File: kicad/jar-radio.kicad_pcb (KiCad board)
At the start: 2 copper layers, 85.5 x 85.5 mm, 64 parts, among them J1 USB-C 5V, J2 BATT (PH), J3 ANT (XH), Q1 AO3401A, U1 Si4825-A10, U2 NS8002, U3 TP4056, U4 XC6206P332MR, U5 XC61CN2702MR, Y1 32.768kHz

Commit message: Speaker on PH socket, USB-C placed by JLC (two-sided), BOM/cost model/plan builder updates
Co-Authored-By: Claude Opus 5.5 <noreply@anthropic.com>
Claude-Session: https://claude.ai/code/session_01UChZ4MGw6SzykNSB399iC4
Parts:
- removed LS1: SPEAKER 8R, jar-radio:Speaker_Wire_Pads_P5
- added J4: SPK (PH), Connector_JST:JST_PH_B2B-PH-SM4-TB_1x02-1MP_P2.00mm_Vertical, B.Cu at (176.0, 100.2)
- moved C19 51.8 mm to (148.2, 133.1)
- moved C20 50.5 mm to (146.1, 133.2), turned to 90 degrees
- moved R14 47.3 mm to (150.6, 129.5)
- moved U3 36.3 mm to (168.2, 101.7), turned to 90 degrees
- moved C13 36.0 mm to (162.8, 131.9), turned to 0 degrees
- moved C12 35.5 mm to (152.5, 124.1)
- moved R12 31.2 mm to (181.6, 86.5)
- moved Q1 30.7 mm to (156.2, 132.9), turned to 0 degrees
- moved R5 20.8 mm to (183.2, 107.0)
- moved R11 19.0 mm to (177.4, 80.2), turned to 180 degrees
- moved C15 17.7 mm to (173.9, 80.0), turned to 0 degrees
- moved C11 15.0 mm to (175.1, 121.1)
- moved RV2 14.2 mm to (180.5, 107.0), turned to 180 degrees
- moved R4 14.1 mm to (163.0, 112.1)
- moved C10 13.4 mm to (182.0, 91.5)
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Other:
- board text added: "ANTENNA"
- board text added: "BATT +/-"
- board text added: "SPEAKER"

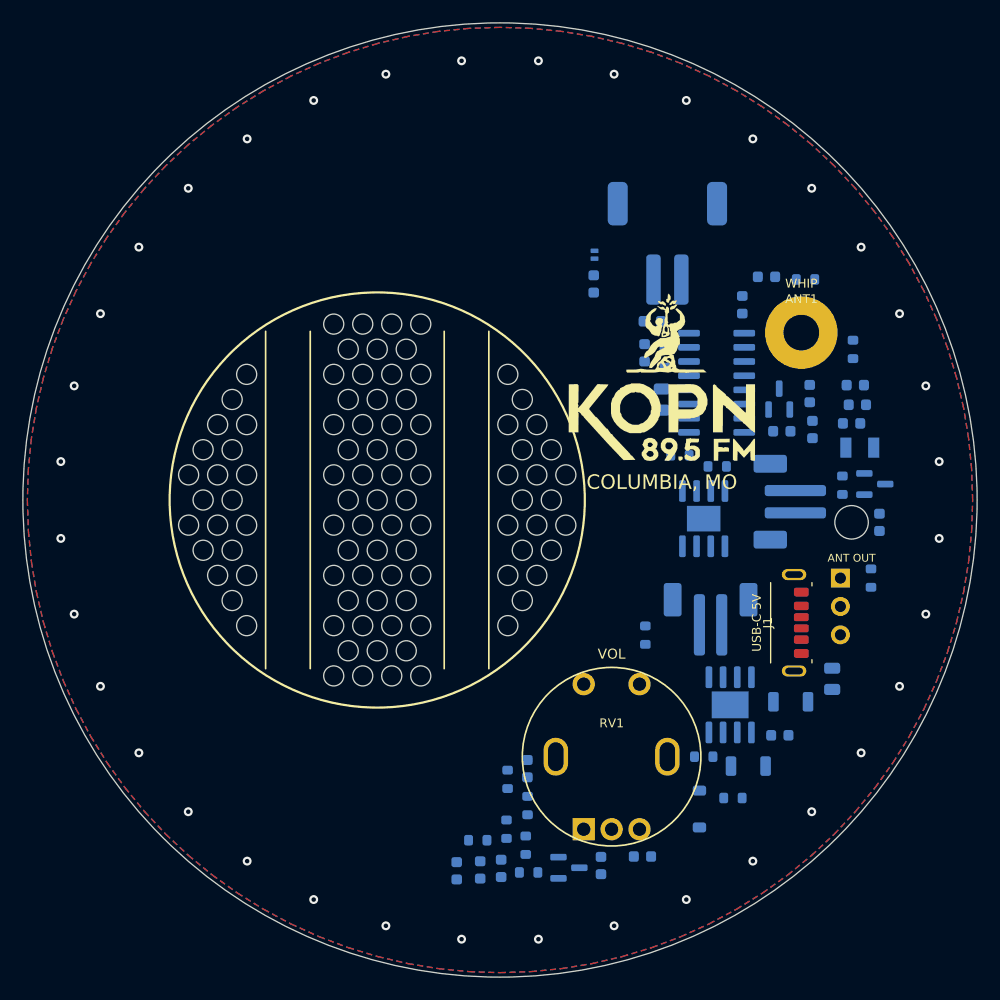
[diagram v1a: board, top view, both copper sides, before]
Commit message: Routed board rev A (one VSW connection still open); session re-import support
Co-Authored-By: Claude Opus 5.5 <noreply@anthropic.com>
Claude-Session: https://claude.ai/code/session_01UChZ4MGw6SzykNSB399iC4
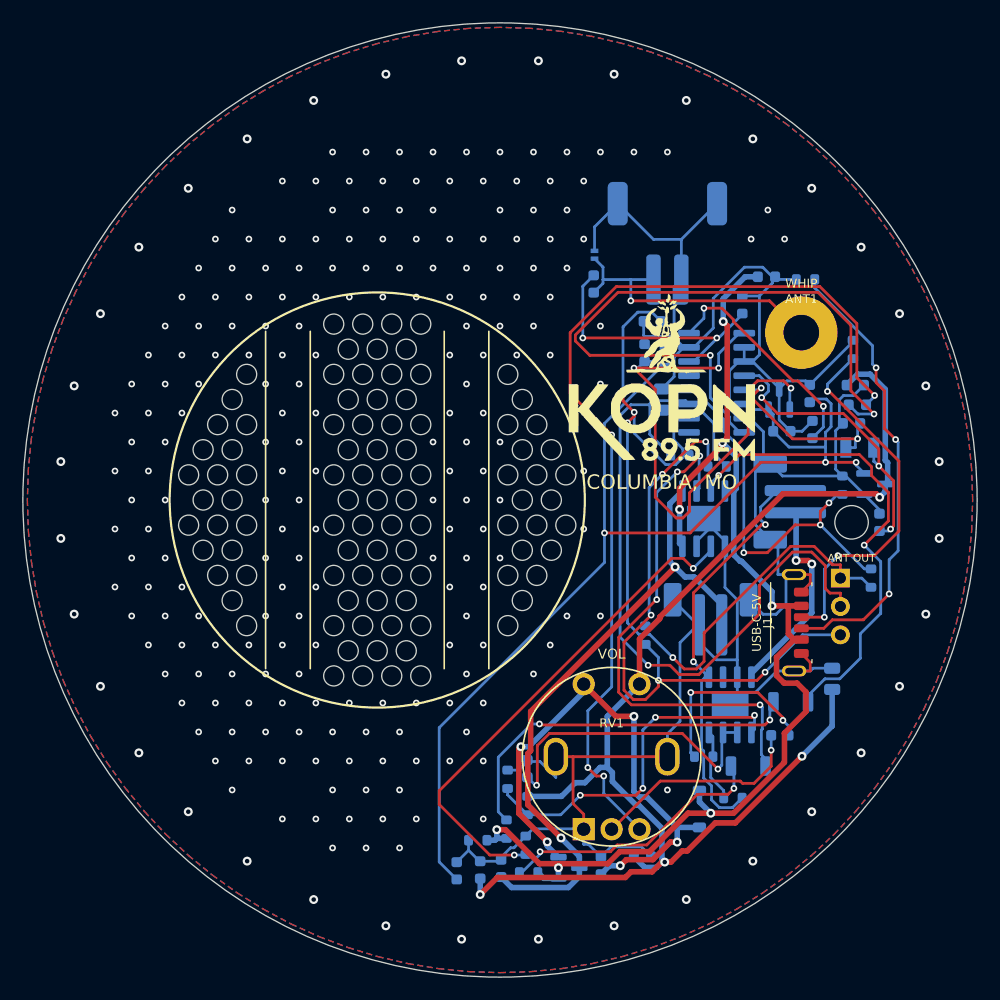
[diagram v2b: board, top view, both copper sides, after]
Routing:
- net GND: track 0.00 -> 246.2 mm, vias 36 -> 244
- net VSW: track 0.00 -> 119.1 mm, vias 0 -> 4
- net VBUS: track 0.00 -> 105.6 mm, vias 0 -> 7
- net +3V3: track 0.00 -> 99.0 mm, vias 0 -> 3
- net VOL_TOP: track 0.00 -> 86.3 mm, vias 0 -> 4
- net TUNE1: track 0.00 -> 78.1 mm, vias 0 -> 4
- net TUNE2: track 0.00 -> 70.4 mm, vias 0 -> 1
- net AOUT: track 0.00 -> 60.5 mm, vias 0 -> 2
- net VBAT: track 0.00 -> 57.8 mm, vias 0 -> 2
- net TUNE_LO: track 0.00 -> 54.5 mm, vias 0 -> 5
- net RST: track 0.00 -> 51.3 mm, vias 0 -> 3
- net VSYS: track 0.00 -> 48.8 mm, vias 0 -> 5
- net STDBY: track 0.00 -> 46.7 mm, vias 0 -> 4
- net PROG: track 0.00 -> 45.3 mm, vias 0 -> 2
- net CHRG: track 0.00 -> 43.3 mm, vias 0 -> 2
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
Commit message: WIP: clear stitching vias near the open VSW connection before final route
Co-Authored-By: Claude Opus 5.5 <noreply@anthropic.com>
Claude-Session: https://claude.ai/code/session_01UChZ4MGw6SzykNSB399iC4
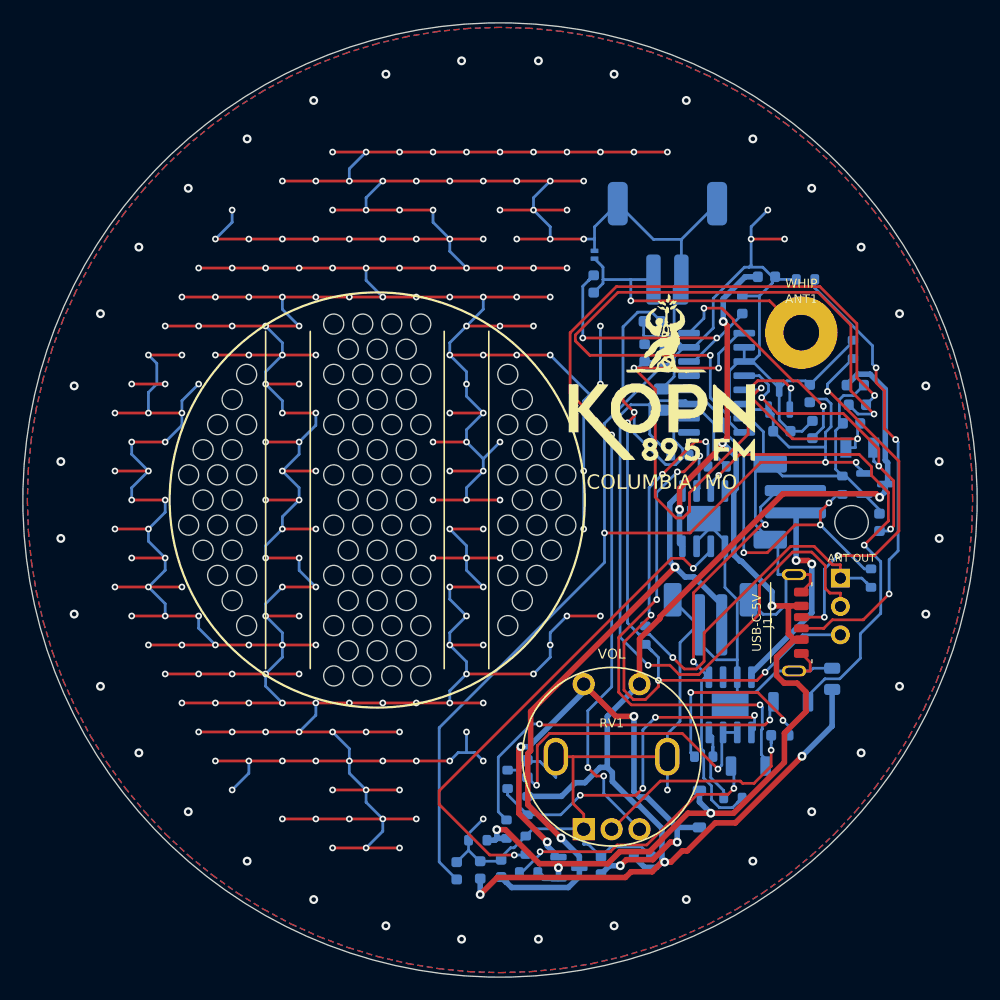
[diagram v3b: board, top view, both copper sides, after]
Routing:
- net GND: track 246.2 -> 893.1 mm
- net TUNE_LO: track 54.5 -> 55.8 mm
- net AMP_INN: track 6.59 -> 7.79 mm
- net VBAT: track 57.8 -> 58.6 mm
- net TUNE2: track 70.4 -> 71.1 mm
- net FMI: track 24.7 -> 25.3 mm
- net VOL_WIPER: track 19.6 -> 20.2 mm
- net XTALO: track 27.1 -> 27.7 mm
- net SPK+: track 37.7 -> 38.3 mm
- net TUNE1: track 78.1 -> 78.7 mm
- net LEDR_A: track 33.5 -> 34.0 mm
- net RST: track 51.3 -> 51.8 mm

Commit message: WIP board state during reroute
Co-Authored-By: Claude Opus 5.5 <noreply@anthropic.com>
Claude-Session: https://claude.ai/code/session_01UChZ4MGw6SzykNSB399iC4
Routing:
- net GND: track 893.1 -> 3.30 mm, vias 244 -> 271
- net AOUT: track 60.5 -> 11.8 mm
- net TUNE1: track 78.7 -> 39.1 mm, vias 4 -> 1
- net TUNE2: track 71.1 -> 31.7 mm
- net RST: track 51.8 -> 26.1 mm, vias 3 -> 4
- net TUNE_LO: track 55.8 -> 37.9 mm, vias 5 -> 3
- net VSYS: track 48.8 -> 32.6 mm, vias 5 -> 0
- net CHRG: track 43.6 -> 29.6 mm
- net VOL_TOP: track 86.3 -> 75.8 mm, vias 4 -> 2
- net VBAT: track 58.6 -> 68.0 mm, vias 2 -> 0
- net VSW: track 119.1 -> 111.5 mm, vias 4 -> 5
- net BAND: track 34.8 -> 27.6 mm, vias 3 -> 2
- net PROG: track 45.3 -> 38.8 mm
- net AMP_C: track 16.9 -> 10.7 mm
- net CC2: track 33.6 -> 39.8 mm, vias 3 -> 1
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
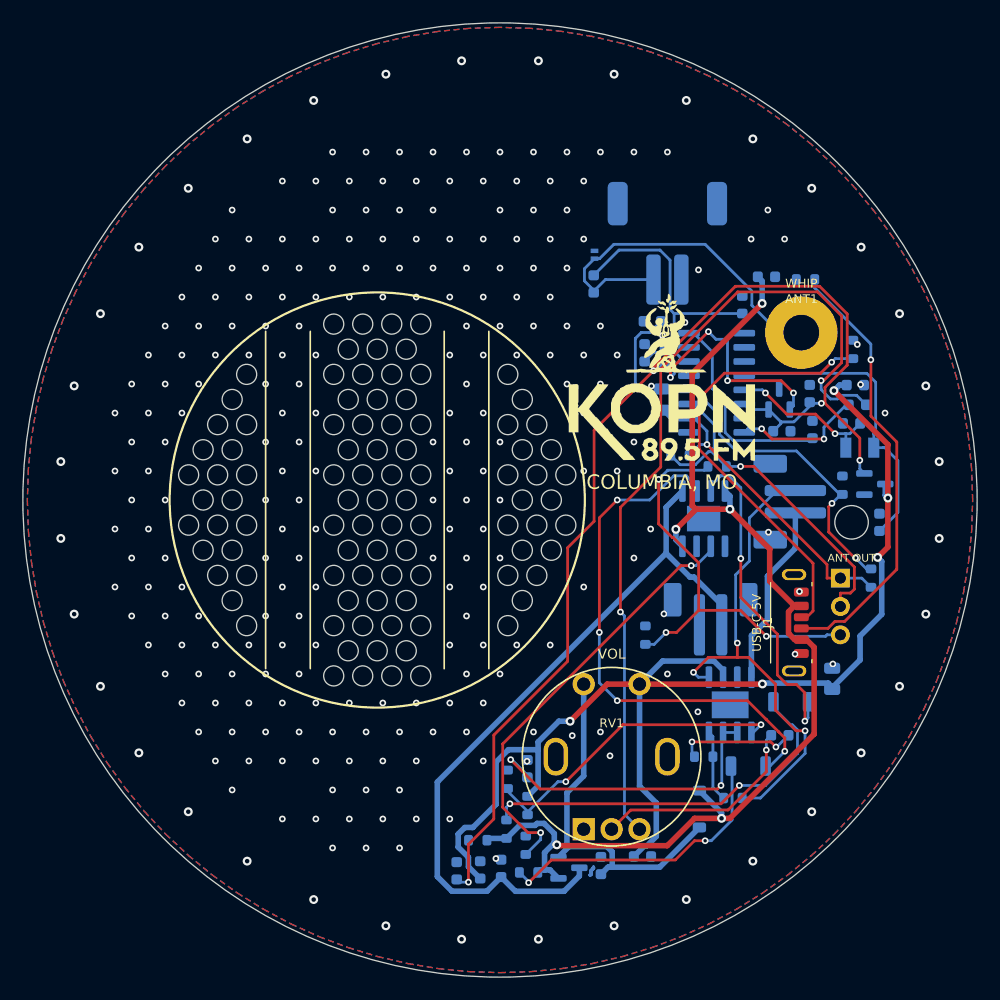
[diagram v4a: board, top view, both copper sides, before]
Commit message: Routed board (pre-stitched GND grid); 14 pour fragments still open; ignore worktrees
Co-Authored-By: Claude Opus 5.5 <noreply@anthropic.com>
Claude-Session: https://claude.ai/code/session_01UChZ4MGw6SzykNSB399iC4
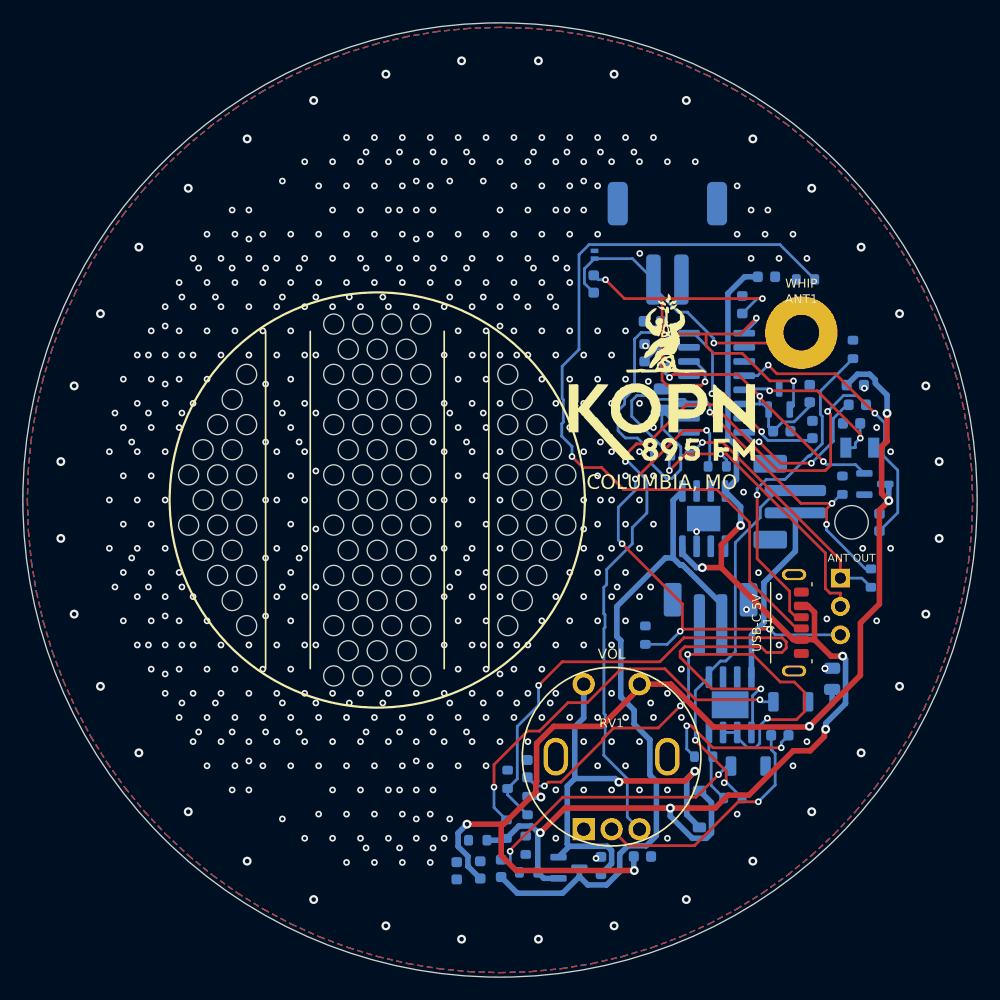
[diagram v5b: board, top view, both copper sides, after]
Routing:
- net +3V3: track 103.2 -> 32.2 mm, vias 4 -> 3
- net STDBY: track 48.0 -> 0.00 mm, vias 4 -> 0
- net PROG: track 38.8 -> 0.00 mm, vias 2 -> 0
- net AMP_SD: track 28.4 -> 61.5 mm
- net CC1: track 39.8 -> 72.0 mm
- net CHRG: track 29.6 -> 0.00 mm, vias 2 -> 0
- net AMP_BYP: track 28.4 -> 46.1 mm, vias 2 -> 4
- net TUNE1: track 39.1 -> 52.8 mm
- net CC2: track 39.8 -> 29.8 mm
- net SPK+: track 43.7 -> 34.5 mm, vias 3 -> 2
- net VBUS: track 101.6 -> 110.6 mm, vias 5 -> 6
- net TUNE_LO: track 37.9 -> 46.3 mm, vias 3 -> 5
- net FMI: track 24.3 -> 32.6 mm, vias 0 -> 3
- net VSYS: track 32.6 -> 40.2 mm, vias 0 -> 2
- net TUNE2: track 31.7 -> 38.9 mm, vias 1 -> 2
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
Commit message: Rev F.2: Alps 20k switched pot, amp gain for 20k pot, 22uF/0603 LED swaps, XC61C pinout fix, JLC quote files
Co-Authored-By: Claude Opus 5.5 <noreply@anthropic.com>
Claude-Session: https://claude.ai/code/session_01UChZ4MGw6SzykNSB399iC4
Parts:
- added C21: 22uF, Capacitor_SMD:C_0805_2012Metric, B.Cu at (165.1, 69.6)
- C11: value 220nF -> 100nF
- C18, C7: value 47uF -> 22uF
- D2, D3: footprint LED_SMD:LED_1206_3216Metric_ReverseMount_Hole1.8x2.4mm -> LED_SMD:LED_0603_1608Metric
- J2: footprint Connector_JST:JST_PH_B2B-PH-SM4-TB_1x02-1MP_P2.00mm_Vertical -> Connector_JST:JST_PH_S2B-PH-SM4-TB_1x02-1MP_P2.00mm_Horizontal
- J4: value SPK (PH) -> SPK (XH); footprint Connector_JST:JST_PH_B2B-PH-SM4-TB_1x02-1MP_P2.00mm_Vertical -> jar-radio:Connector_XH-SMD_GSwitch_GT-A2501WRS-102_1x02_P2.50mm_Horizontal
- R7: value 22k -> 47k
- R8: value 220k -> 560k
- RV1: value B50K + SW -> 20k + SW
- moved C19 52.7 mm to (184.2, 94.7)
- moved C12 29.7 mm to (179.6, 112.0)
- moved R11 27.6 mm to (181.9, 107.5)
- moved C13 27.5 mm to (181.8, 112.1), turned to 90 degrees
- moved J2 27.0 mm to (150.0, 130.0), turned to 0 degrees
- moved Q1 25.0 mm to (176.8, 118.9)
- moved C15 24.0 mm to (184.2, 101.7), turned to 90 degrees
- moved U4 22.6 mm to (172.6, 118.3)
- moved U1 22.3 mm to (155.1, 72.4)
- moved U3 21.5 mm to (171.0, 123.0), turned to 180 degrees
- moved D2 21.2 mm to (183.6, 98.3), turned to 90 degrees
- moved C14 19.6 mm to (181.6, 109.3)
- moved R12 18.8 mm to (184.3, 105.1)
- moved R9 18.0 mm to (168.6, 127.0), turned to 0 degrees
- moved R5 17.5 mm to (166.0, 104.0), turned to 0 degrees
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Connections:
- U5 pad 2: +3V3 -> GND
- U5 pad 3: GND -> +3V3
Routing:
- net VBUS: track 110.6 -> 0.00 mm, vias 6 -> 0
- net VSW: track 108.5 -> 0.00 mm, vias 6 -> 0
- net CC1: track 72.0 -> 0.00 mm, vias 1 -> 0
- net VOL_TOP: track 69.9 -> 0.00 mm, vias 2 -> 0
- net VBAT: track 62.1 -> 0.00 mm
- net AMP_SD: track 61.5 -> 0.00 mm, vias 2 -> 0
- net TUNE1: track 52.8 -> 0.00 mm, vias 1 -> 0
- net TUNE_LO: track 46.3 -> 0.00 mm, vias 5 -> 0
- net AMP_BYP: track 46.1 -> 0.00 mm, vias 4 -> 0
- net VSYS: track 40.2 -> 0.00 mm, vias 2 -> 0
- net TUNE2: track 38.9 -> 0.00 mm, vias 2 -> 0
- net LEDR_A: track 35.2 -> 0.00 mm, vias 2 -> 0
- net SPK+: track 34.5 -> 0.00 mm, vias 2 -> 0
- net FMI: track 32.6 -> 0.00 mm, vias 3 -> 0
- net +3V3: track 32.2 -> 0.00 mm, vias 3 -> 0
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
